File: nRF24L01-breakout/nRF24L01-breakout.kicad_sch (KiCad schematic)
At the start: 19 parts, among them J1 Conn_01x08_Female, U1 NRF24L01, U2 Antenna_PCB_2.4GHz_50Ohm, Y1 16MHz

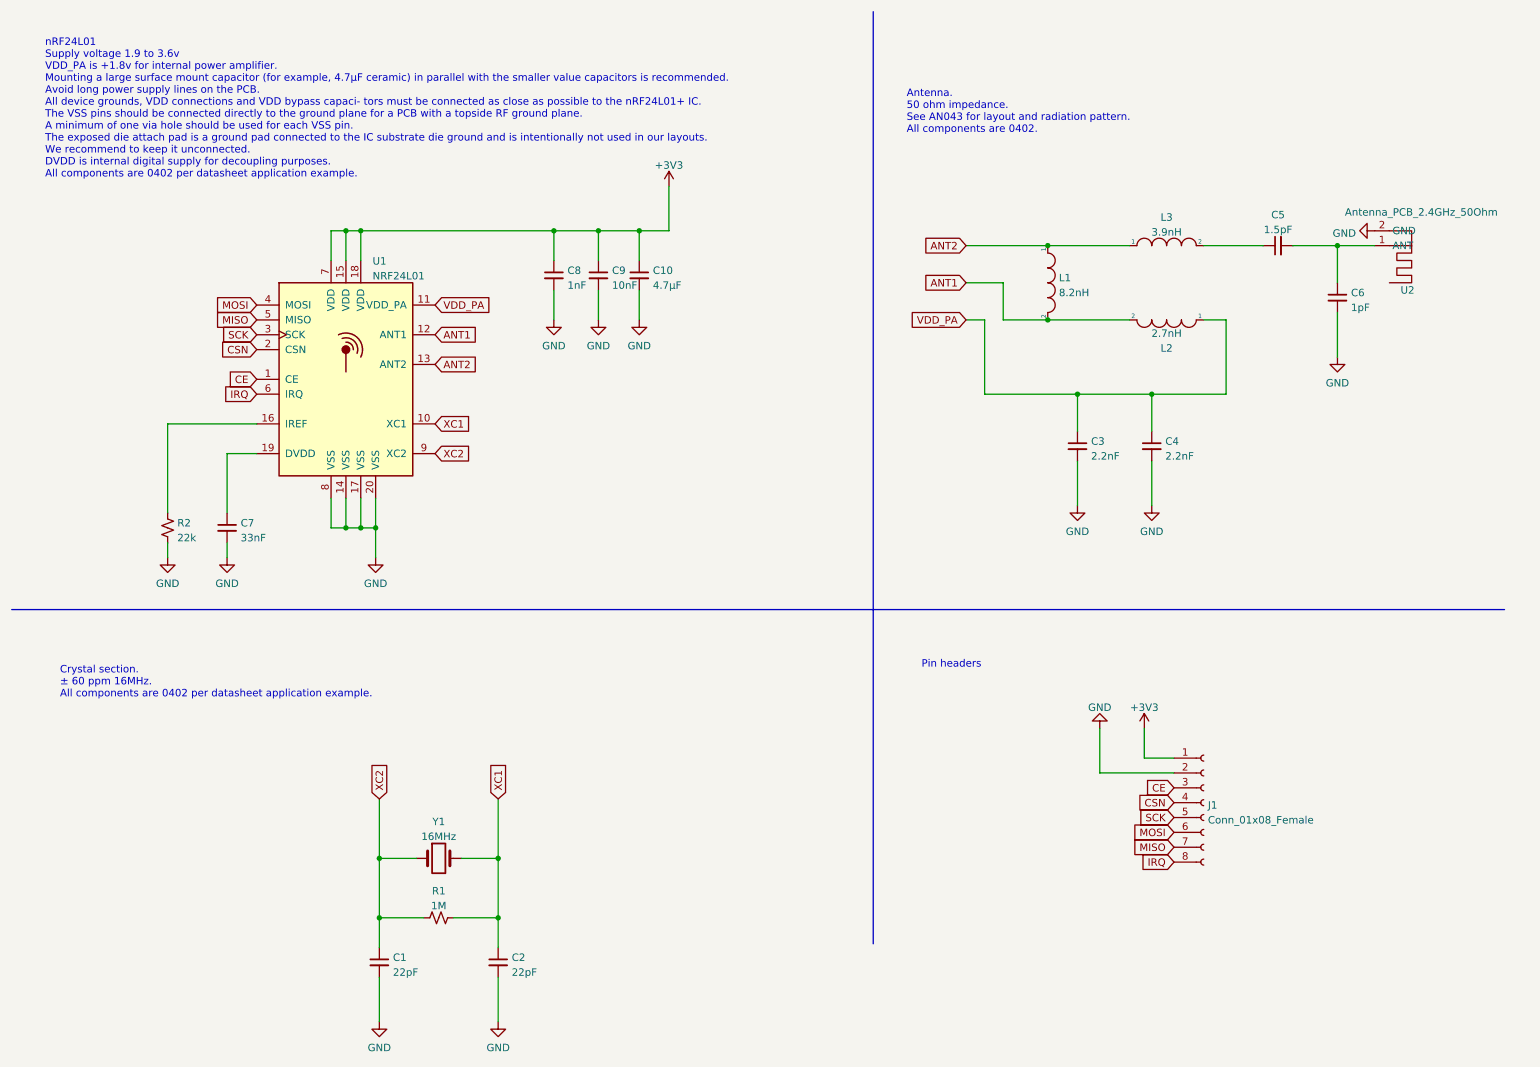
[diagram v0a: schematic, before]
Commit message: Use Johanson 2450BM14A0002 matched balun
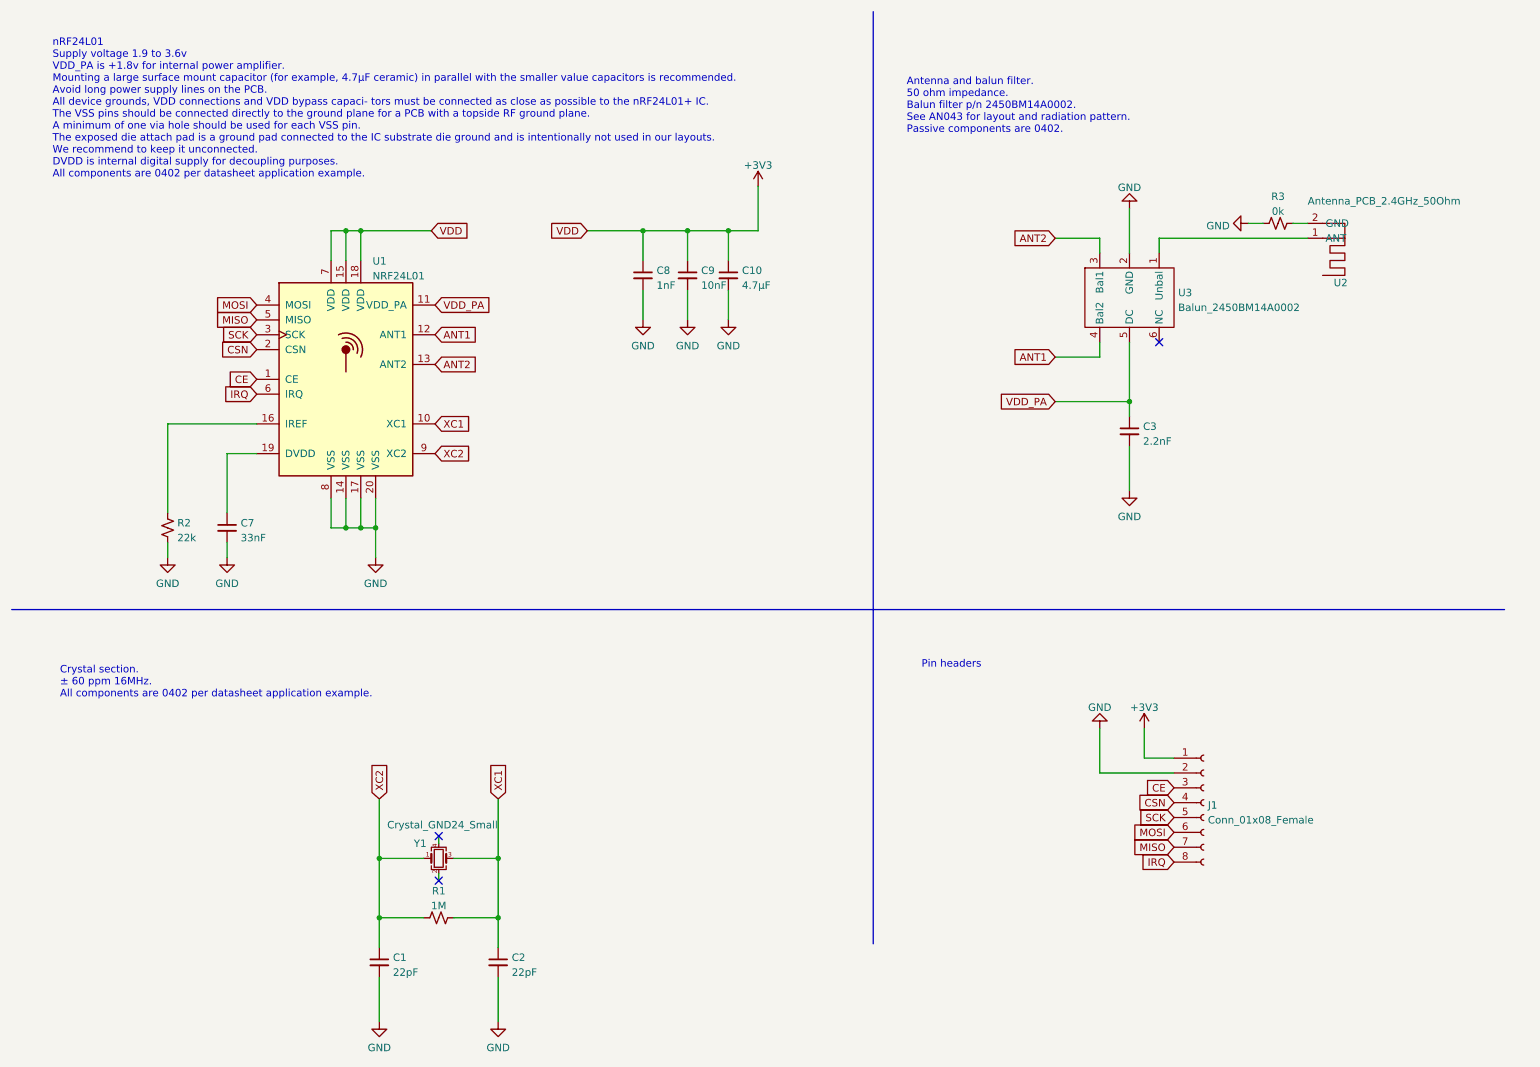
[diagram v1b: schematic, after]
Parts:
- removed C4: 2.2nF, Capacitor_SMD:C_0402_1005Metric, symbol Device:C_Small
- removed C5: 1.5pF, Capacitor_SMD:C_0402_1005Metric, symbol Device:C_Small
- removed C6: 1pF, Capacitor_SMD:C_0402_1005Metric, symbol Device:C_Small
- removed L1: 8.2nH, Inductor_SMD:L_0402_1005Metric, symbol pspice:INDUCTOR
- removed L2: 2.7nH, Inductor_SMD:L_0402_1005Metric, symbol pspice:INDUCTOR
- removed L3: 3.9nH, Inductor_SMD:L_0402_1005Metric, symbol pspice:INDUCTOR
- removed Y1: 16MHz, Crystal:Resonator-2Pin_W6.0mm_H3.0mm, symbol Device:Crystal
- added R3: 0k, Resistor_SMD:R_0603_1608Metric, symbol Device:R_Small_US
- added U3: Balun_2450BM14A0002, RF_Converter:Balun_Johanson_0896BM15A0001, symbol Custom:Balun_2450BM14A0002
- added Y1: Crystal_GND24_Small, Crystal:Crystal_SMD_2520-4Pin_2.5x2.0mm, symbol Device:Crystal_GND24_Small
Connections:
- net ANT1: now also U3.4 (Bal2)
- net ANT2: now also U3.3 (Bal1)
- net GND: now also R3.2, U3.2 (GND); no longer U2.2 (GND)
- net VDD_PA: now also U3.5 (DC)
- net XC1: now also Y1.3
- net XC2: now also Y1.1
- net at U2.1 (ANT): now also U3.1 (Unbal)
- new net: R3.1, U2.2 (GND)
- no-connect marks 0 -> 3
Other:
- note added: "Antenna and balun filter. 50 ohm impedance. Balun filter p/n 2450BM14A0002. See AN043 for layout and radiation pattern. Passive components are 0402."
- note removed: "Antenna. 50 ohm impedance. See AN043 for layout and radiation pattern. All components are 0402."
- moved on the sheet: C10, C3, C8, C9, U2
